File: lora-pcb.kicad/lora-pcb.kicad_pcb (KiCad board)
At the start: 2 copper layers, 36.5 x 33 mm, 11 parts, among them J1 Conn_SUR, J2 Conn_THT, U1 RFM95W-868S2

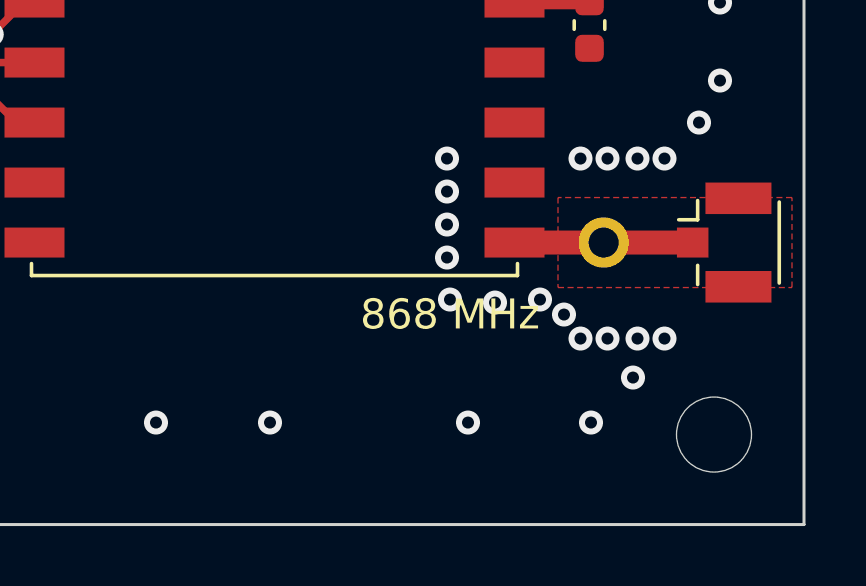
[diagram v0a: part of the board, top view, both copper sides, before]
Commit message: LoRa-PCB Rev 1.00: version with 433MHz (ready for production)
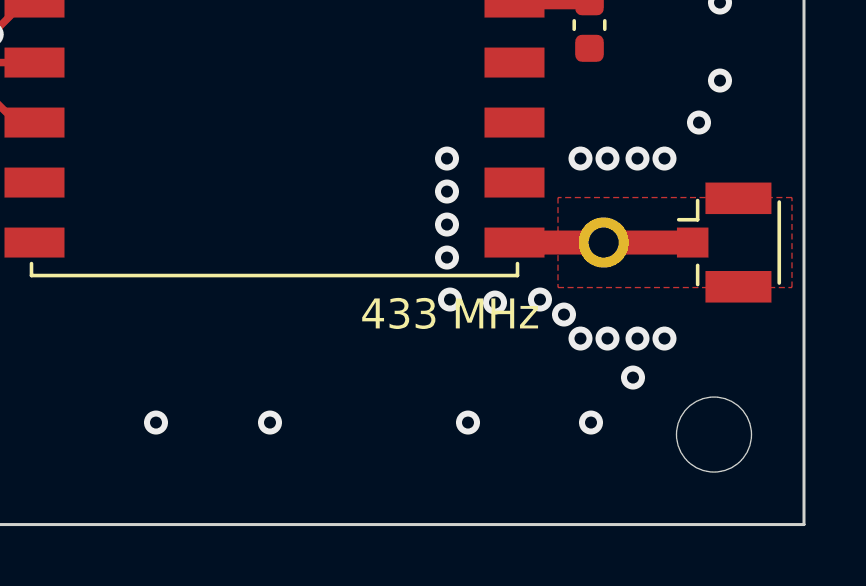
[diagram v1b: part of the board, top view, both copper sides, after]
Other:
- board text added: "433 MHz"
- board text added: "https://github.com/bablokb/ pcb-pico-datalogger Rev: 1.00"
- board text removed: "868 MHz"
- board text removed: "https://github.com/bablokb/ pcb-pico-datalogger Rev: 0.90"
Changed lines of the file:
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@@
     (descr "Low Power Long Range Transceiver Module SMD-16 (https://www.hoperf.com/data/upload/portal/20181127/5bfcbea20e9ef.pdf)")
     (tags "LoRa Low Power Long Range Transceiver Module")
-    (property "LCSC" "C2844472")
+    (property "LCSC" "C2844474")
     (property "Sheetfile" "lora-pcb.kicad_sch")
     (property "Sheetname" "")
@@
     (effects (font (size 1 1) (thickness 0.15)) (justify left mirror))
   )
-  (gr_text "https://github.com/bablokb/\n          pcb-pico-datalogger\nRev: 0.90" (at 130.5 130.3) (layer "B.SilkS")
+  (gr_text "https://github.com/bablokb/\n          pcb-pico-datalogger\nRev: 1.00" (at 130.5 130.3) (layer "B.SilkS")
     (effects (font (size 1 1) (thickness 0.15)) (justify left mirror))
   )
@@
     (effects (font (size 1 1) (thickness 0.15)))
   )
-  (gr_text "868 MHz" (at 124.7 126) (layer "F.SilkS")
+  (gr_text "433 MHz" (at 124.7 126) (layer "F.SilkS")
     (effects (font (size 1 1) (thickness 0.15)))
   )

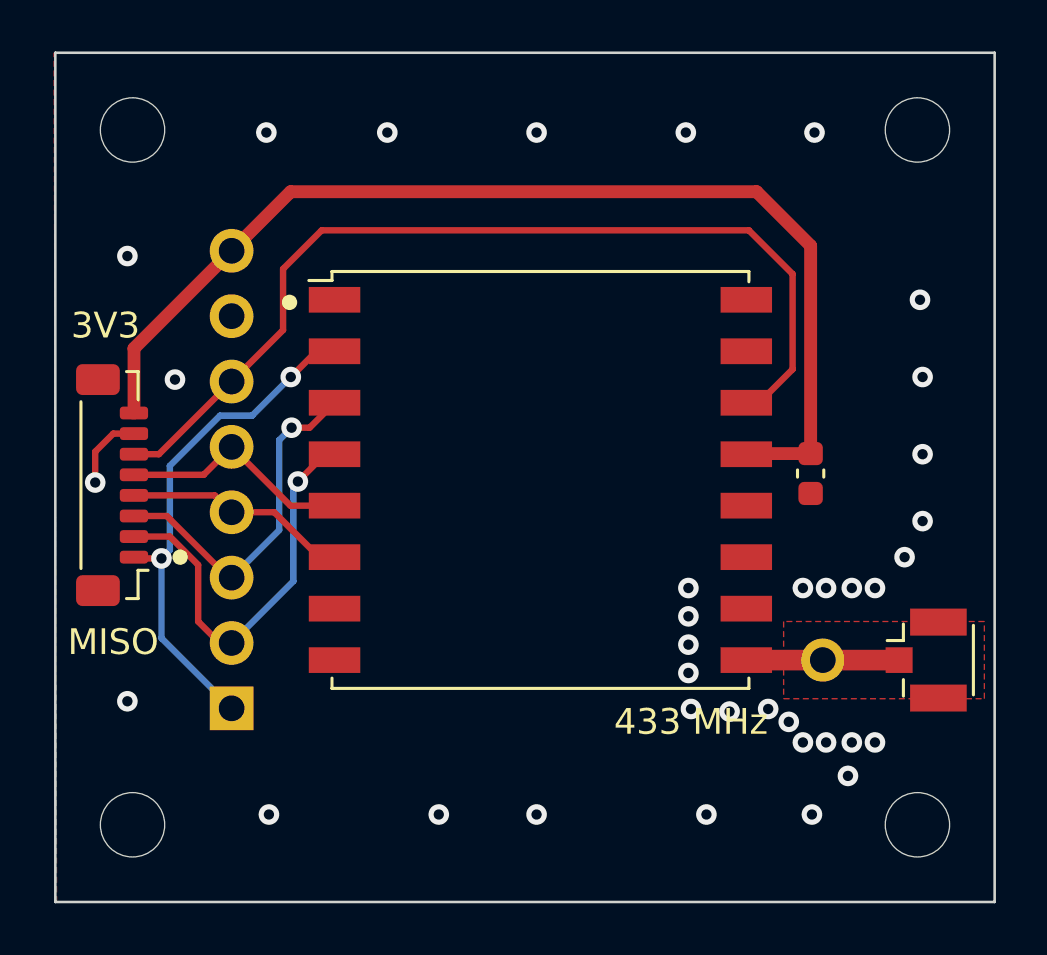
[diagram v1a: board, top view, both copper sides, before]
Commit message: RoRa-PCB Rev 1.10: turn SURS adapter
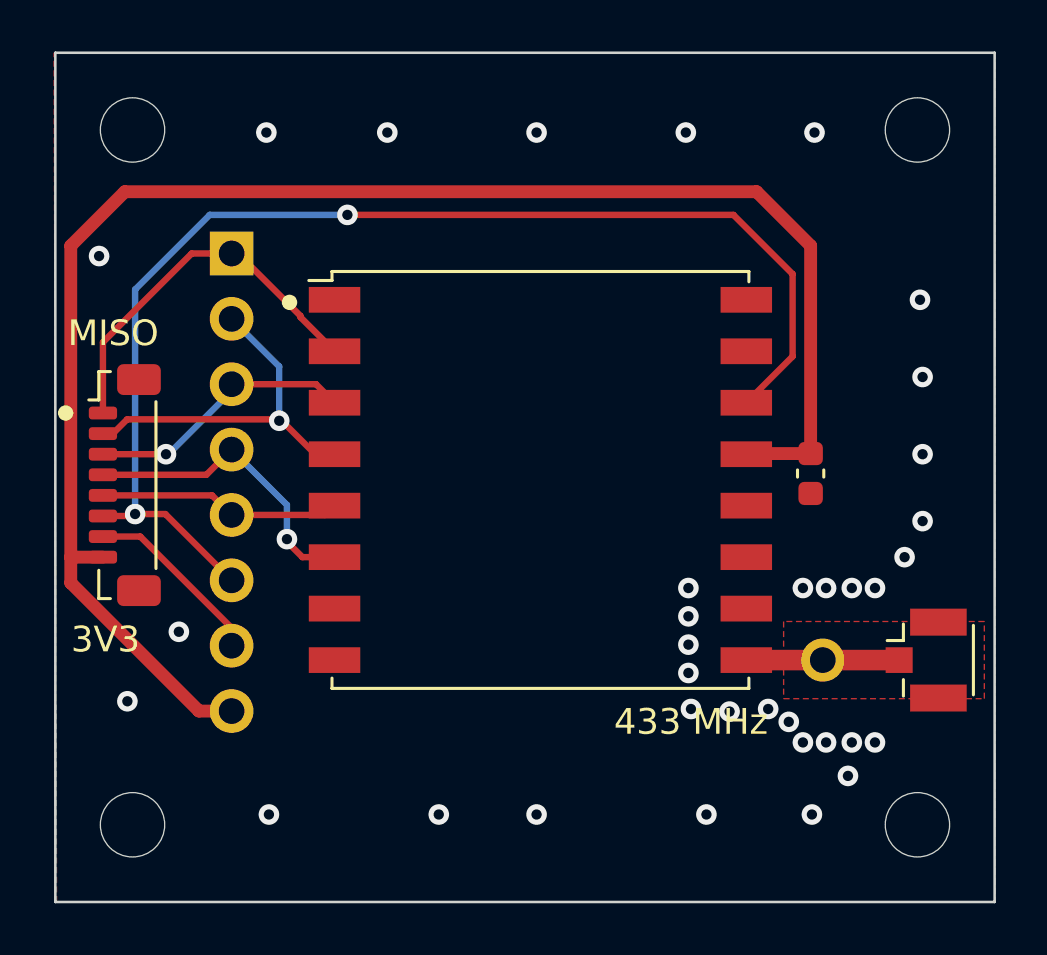
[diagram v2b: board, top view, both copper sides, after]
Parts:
- moved J2 17.7 mm to (106.8, 107.8), turned to 180 degrees
- moved J1 0.49 mm to (102.7, 116.8), turned to -90 degrees
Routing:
- net +3V3: track 42.8 -> 63.7 mm
- net /Lora_DIO0: track 37.3 -> 48.3 mm, vias 0 -> 2
- net /MISO1: track 19.9 -> 14.8 mm, vias 2 -> 0
- net GND: track 3.00 -> 7.16 mm, vias 36 -> 35
- net /Lora_RST: track 8.79 -> 12.0 mm, vias 0 -> 1
- net /MOSI1: track 13.7 -> 10.6 mm
- net /SCLK1: track 16.0 -> 14.5 mm
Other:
- board text added: "https://github.com/bablokb/ pcb-pico-datalogger Rev: 1.10"
- board text removed: "https://github.com/bablokb/ pcb-pico-datalogger Rev: 1.00"
